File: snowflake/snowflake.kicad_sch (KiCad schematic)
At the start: 70 parts, among them J1 Conn_01x05_Pin, J2 Conn_01x04_Pin, U1 TZ-5050S2RGB-5V-I4-H1, U10 TZ-5050S2RGB-5V-I4-H1, U11 TZ-5050S2RGB-5V-I4-H1, U12 TZ-5050S2RGB-5V-I4-H1, U13 TZ-5050S2RGB-5V-I4-H1, U14 TZ-5050S2RGB-5V-I4-H1, U15 TZ-5050S2RGB-5V-I4-H1, U16 TZ-5050S2RGB-5V-I4-H1, U17 TZ-5050S2RGB-5V-I4-H1, U18 TZ-5050S2RGB-5V-I4-H1, U19 TZ-5050S2RGB-5V-I4-H1, U2 TZ-5050S2RGB-5V-I4-H1, U20 TZ-5050S2RGB-5V-I4-H1, U21 TZ-5050S2RGB-5V-I4-H1, U22 TZ-5050S2RGB-5V-I4-H1, U23 TZ-5050S2RGB-5V-I4-H1, U24 TZ-5050S2RGB-5V-I4-H1, U25 TPS61022, U26 CH32V003F4U6, U3 TZ-5050S2RGB-5V-I4-H1, U4 TZ-5050S2RGB-5V-I4-H1, U5 TZ-5050S2RGB-5V-I4-H1, U6 TZ-5050S2RGB-5V-I4-H1, U7 TZ-5050S2RGB-5V-I4-H1, U8 TZ-5050S2RGB-5V-I4-H1, U9 TZ-5050S2RGB-5V-I4-H1

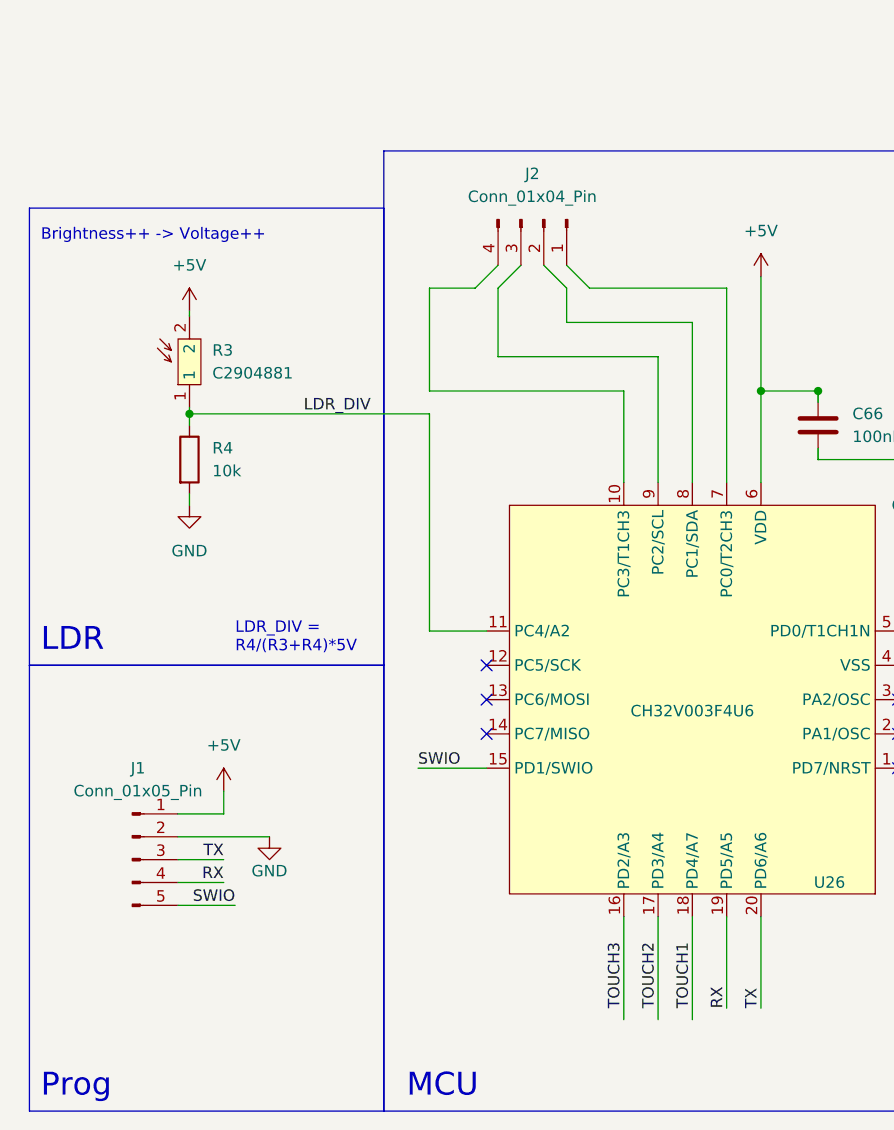
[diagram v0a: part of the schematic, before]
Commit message: Update PCB and customize some footprints
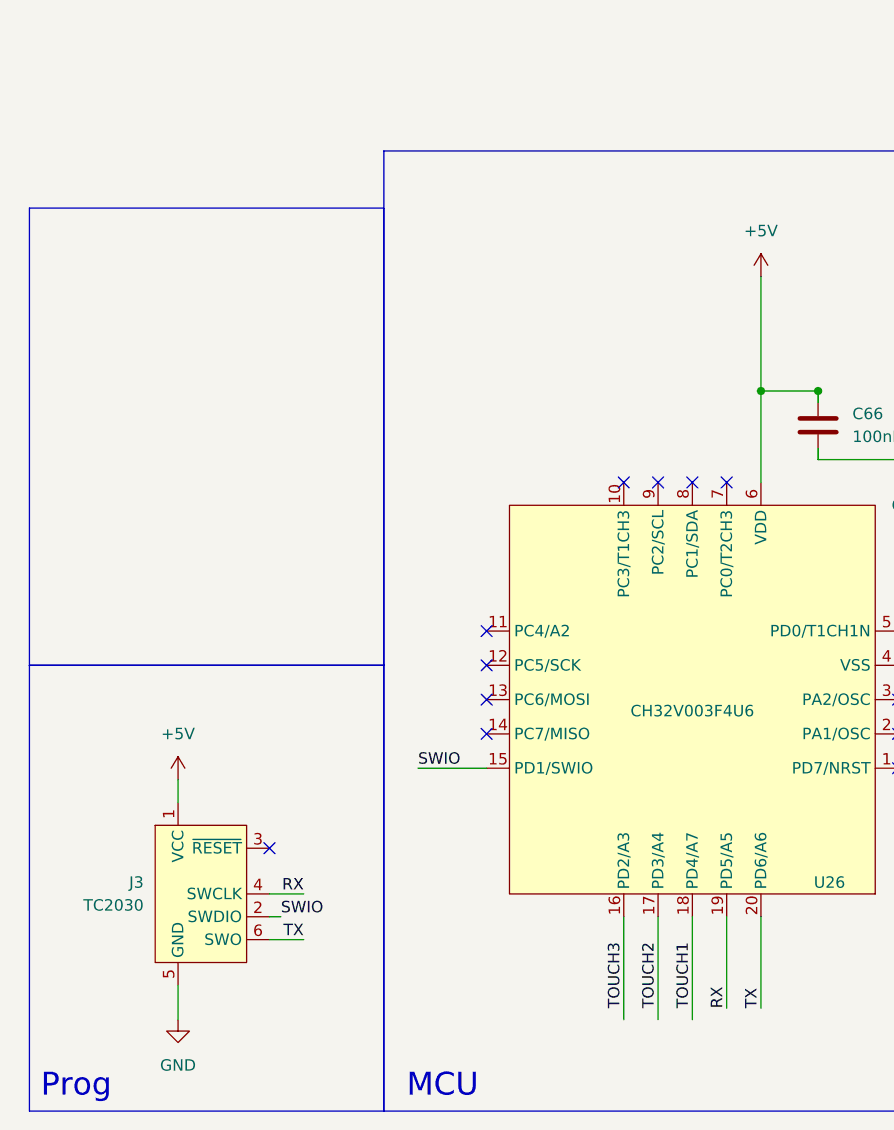
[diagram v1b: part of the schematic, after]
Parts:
- removed J1: Conn_01x05_Pin, Connector_PinHeader_2.54mm:PinHeader_1x05_P2.54mm_Vertical, symbol Connector:Conn_01x05_Pin
- removed J2: Conn_01x04_Pin, Connector_PinHeader_2.54mm:PinHeader_1x04_P2.54mm_Vertical, symbol Connector:Conn_01x04_Pin
- removed R3: C2904881, easyeda2kicad:RES-SMD_L3.6-W2.4, symbol easyeda2kicad:GT36528
- removed R4: 10k, Resistor_SMD:R_0603_1608Metric, symbol Device:R
- added J3: TC2030, Connector:Tag-Connect_TC2030-IDC-NL_2x03_P1.27mm_Vertical, symbol Connector:Conn_ARM_SWD_TagConnect_TC2030-NL
- BAT1: footprint easyeda2kicad:BAT-TH_2P-P14.50_2462 -> snowflake:BAT-TH_2P-P14.50_2462
- C66: footprint Capacitor_SMD:C_0402_1005Metric -> snowflake:C_0402_1005Metric
- TP5, TP6, TP7: footprint TestPoint:TestPoint_Pad_D2.0mm -> snowflake:TestPoint_Pad_D2.0mm
- U25: footprint easyeda2kicad:VQFN-7_L2.0-W2.0-P0.55-TL_RWU -> snowflake:VQFN-7_L2.0-W2.0-P0.55-TL_RWU
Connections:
- net +5V: now also J3.1 (VCC)
- net GND: now also J3.5 (GND)
- net RX: now also J3.4 (SWCLK)
- net SWIO: now also J3.2 (SWDIO)
- net TX: now also J3.6 (SWO)
- net LDR_DIV: no longer names the net of U26.11 (PC4/A2)
- no-connect marks 8 -> 14
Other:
- note removed: "Brightness++ -> Voltage++"
- note removed: "LDR"
- note removed: "LDR_DIV = R4/(R3+R4)*5V"

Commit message: Add graphics to board
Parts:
- added J1: Conn_01x02_Pin, Connector_PinHeader_2.54mm:PinHeader_1x02_P2.54mm_Vertical, symbol Connector:Conn_01x02_Pin
- L1: LCSC Part (none) -> C5179444
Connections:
- net BAT+: now also S1.3; no longer S1.2
- net DIN: now also J1.1 (Pin_1)
- net EN: now also S1.2; no longer S1.1
- net GND: now also S1.1
- net SWIO: now also J3.6 (SWO); no longer J3.2 (SWDIO)
- net TX: now also J3.2 (SWDIO); no longer J3.6 (SWO)
- net Vdd: now reaches R1.2, R2.1
- net Vdd: now also C1.2, C10.2, C11.2, C12.2, C13.2, C14.2, C15.2, C16.2, C17.2, C18.2, C19.2, C2.2, C20.2, C21.2, C22.2, C23.2, C24.2, C25.1, C26.1, C3.2, C4.2, C5.2, C6.2, C66.1, C7.2, C8.2, C9.2, J3.1 (VCC), R5.1, R6.1, R7.1, U1.1 (VDD), U10.1 (VDD), U11.1 (VDD), U12.1 (VDD), U13.1 (VDD), U14.1 (VDD), U15.1 (VDD), U16.1 (VDD), U17.1 (VDD), U18.1 (VDD), U19.1 (VDD), U2.1 (VDD), U20.1 (VDD), U21.1 (VDD), U22.1 (VDD), U23.1 (VDD), U24.1 (VDD), U25.3 (VOUT), U26.6 (VDD), U3.1 (VDD), U4.1 (VDD), U5.1 (VDD), U6.1 (VDD), U7.1 (VDD), U8.1 (VDD), U9.1 (VDD), J1.2 (Pin_2); no longer U25.4 (FB)
- removed net +5V: C1.2, C10.2, C11.2, C12.2, C13.2, C14.2, C15.2, C16.2, C17.2, C18.2, C19.2, C2.2, C20.2, C21.2, C22.2, C23.2, C24.2, C25.1, C26.1, C3.2, C4.2, C5.2, C6.2, C66.1, C7.2, C8.2, C9.2, J3.1 (VCC), R0.2, R5.1, R6.1, R7.1, U1.1 (VDD), U10.1 (VDD), U11.1 (VDD), U12.1 (VDD), U13.1 (VDD), U14.1 (VDD), U15.1 (VDD), U16.1 (VDD), U17.1 (VDD), U18.1 (VDD), U19.1 (VDD), U2.1 (VDD), U20.1 (VDD), U21.1 (VDD), U22.1 (VDD), U23.1 (VDD), U24.1 (VDD), U25.3 (VOUT), U26.6 (VDD), U3.1 (VDD), U4.1 (VDD), U5.1 (VDD), U6.1 (VDD), U7.1 (VDD), U8.1 (VDD), U9.1 (VDD)
- new net FB: R0.2, U25.4 (FB)
- no-connect marks 14 -> 13
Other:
- note added: "((510k + 220k)/100k + 1) * 0.6 = 4.98v"
- note added: "Batt / Power Switch"
- note removed: "Batt"
- moved on the sheet: C1, C10, C11, C12, C13, C14, C15, C16, C17, C18, C19, C2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
